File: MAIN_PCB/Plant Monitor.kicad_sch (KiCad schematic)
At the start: 59 parts, among them J1 TYPE-C-31-M-12, J2 Motor 1, J3 Motor 2, J4 Grove Connector for Soil Mois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, J5 Grove Connector for OLED Disp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, J6 Conn_01x14, J7 Conn_01x14, J8 JST PH-2Pin, J9 BME280 Terminals, Q1 AO3401A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

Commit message: Revision D of PCB design
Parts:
- U4: footprint Package_SON:Winbond_USON-8-1EP_3x2mm_P0.5mm_EP0.2x1.6mm -> Package_SO:SOIC-8_5.3x5.3mm_P1.27mm
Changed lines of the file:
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@@
 			)
 		)
-		(property "Footprint" "Package_SON:Winbond_USON-8-1EP_3x2mm_P0.5mm_EP0.2x1.6mm"
+		(property "Footprint" "Package_SO:SOIC-8_5.3x5.3mm_P1.27mm"
 			(at 321.31 218.44 0)
 			(hide yes)

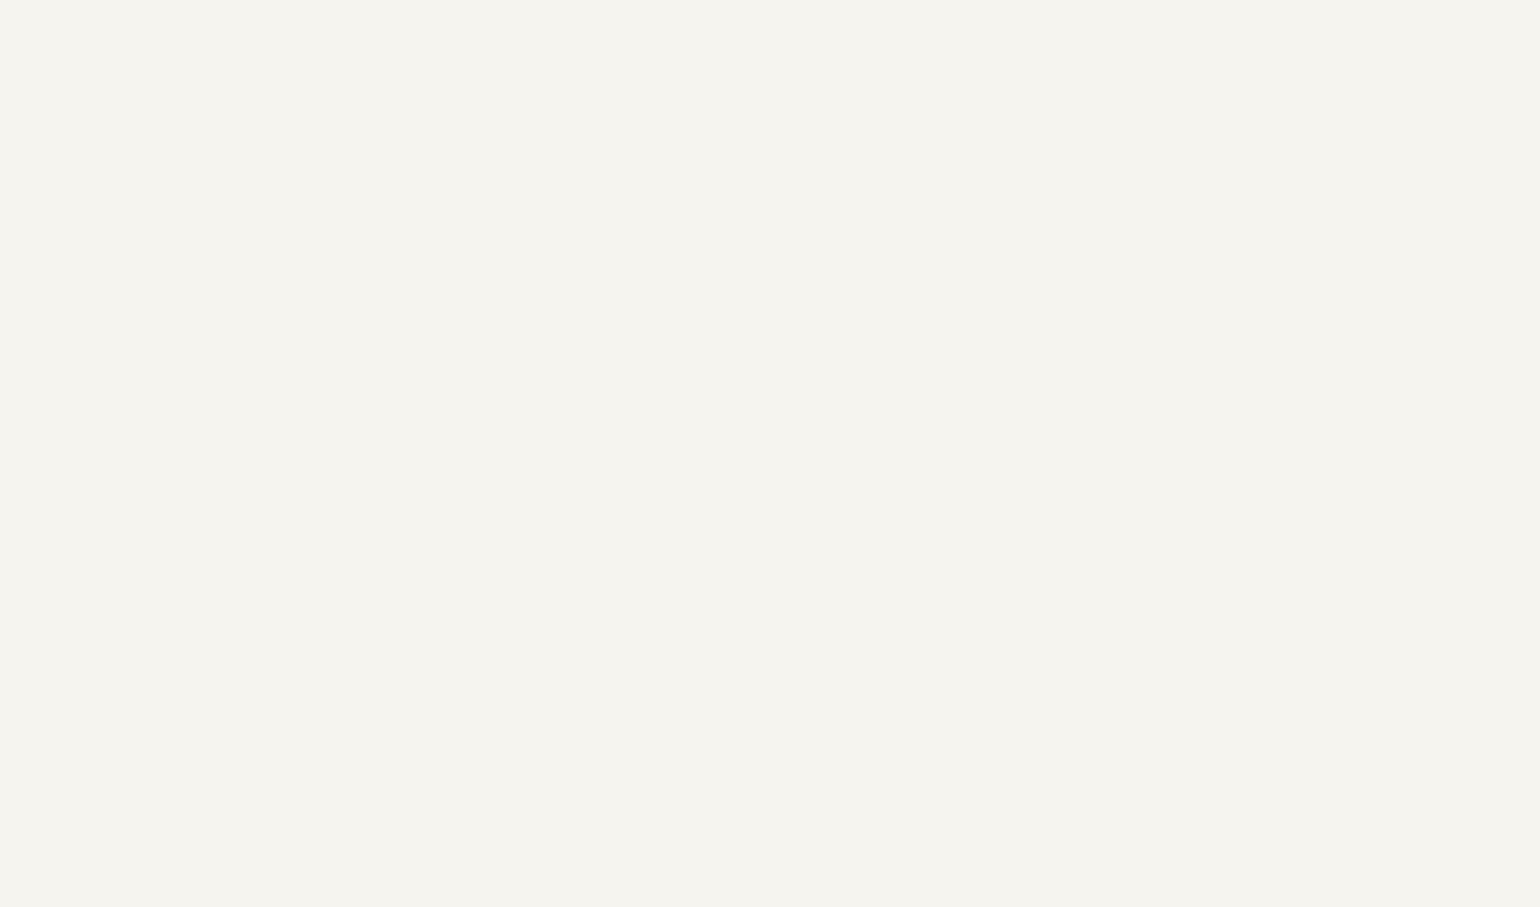
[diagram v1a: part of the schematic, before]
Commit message: Added wiring/schematic
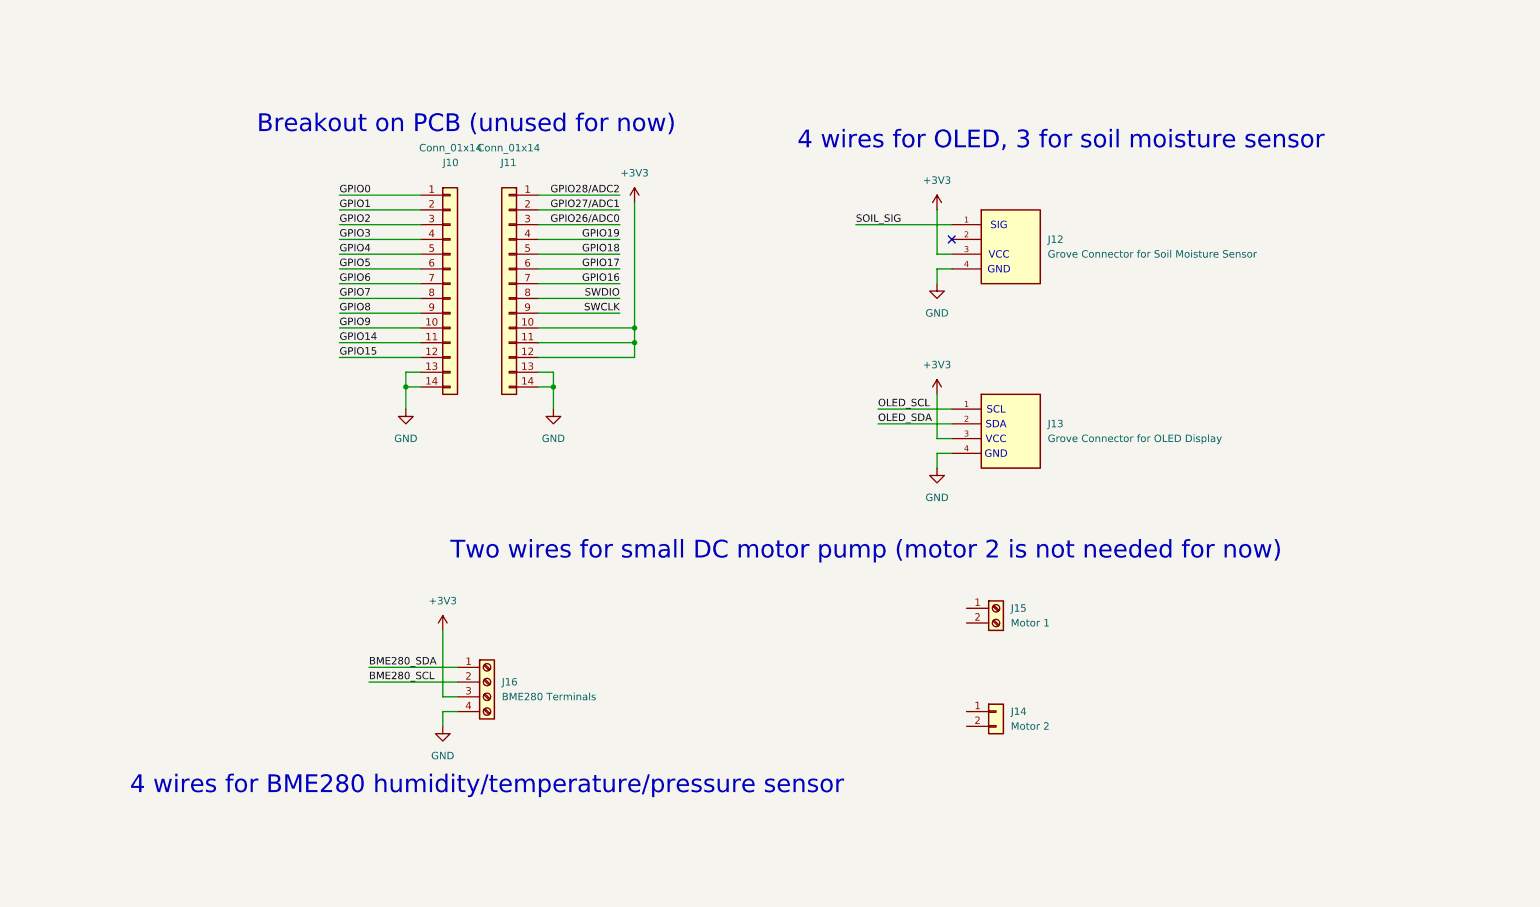
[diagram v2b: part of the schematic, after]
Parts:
- added J10, J11: Conn_01x14, Connector_PinHeader_2.54mm:PinHeader_1x14_P2.54mm_Vertical, symbol Connector_Generic:Conn_01x14
- added J12: Grove Connector for Soil Moisture Sensor, ExternalFootprints:SEEED_110990030, symbol Grove 4Pin Connector:110990030
- added J13: Grove Connector for OLED Display, ExternalFootprints:SEEED_110990030, symbol Grove 4Pin Connector:110990030
- added J14: Motor 2, Connector_PinHeader_2.54mm:PinHeader_1x02_P2.54mm_Vertical, symbol Connector_Generic:Conn_01x02
- added J15: Motor 1, TerminalBlock_Phoenix:TerminalBlock_Phoenix_MKDS-1,5-2-5.08_1x02_P5.08mm_Horizontal, symbol Connector:Screw_Terminal_01x02
- added J16: BME280 Terminals, TerminalBlock_Phoenix:TerminalBlock_Phoenix_MKDS-1,5-4_1x04_P5.00mm_Horizontal, symbol Connector:Screw_Terminal_01x04
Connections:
- net +3V3: now also J11.10 (Pin_10), J11.11 (Pin_11), J11.12 (Pin_12), J12.3, J13.3, J16.3 (Pin_3)
- net BME280_SCL: now also J16.2 (Pin_2)
- net BME280_SDA: now also J16.1 (Pin_1)
- net GND: now also J10.13 (Pin_13), J10.14 (Pin_14), J11.13 (Pin_13), J11.14 (Pin_14), J12.4, J13.4, J16.4 (Pin_4)
- net GPIO0: now also J10.1 (Pin_1)
- net GPIO1: now also J10.2 (Pin_2)
- net GPIO14: now also J10.11 (Pin_11)
- net GPIO15: now also J10.12 (Pin_12)
- net GPIO16: now also J11.7 (Pin_7)
- net GPIO17: now also J11.6 (Pin_6)
- net GPIO18: now also J11.5 (Pin_5)
- net GPIO19: now also J11.4 (Pin_4)
- net GPIO2: now also J10.3 (Pin_3)
- net GPIO26/ADC0: now also J11.3 (Pin_3)
- net GPIO27/ADC1: now also J11.2 (Pin_2)
- net GPIO28/ADC2: now also J11.1 (Pin_1)
- net GPIO3: now also J10.4 (Pin_4)
- net GPIO4: now also J10.5 (Pin_5)
- net GPIO5: now also J10.6 (Pin_6)
- net GPIO6: now also J10.7 (Pin_7)
- net GPIO7: now also J10.8 (Pin_8)
- net GPIO8: now also J10.9 (Pin_9)
- net GPIO9: now also J10.10 (Pin_10)
- net OLED_SCL: now also J13.1
- net OLED_SDA: now also J13.2
- net SOIL_SIG: now also J12.1
- net SWCLK: now also J11.9 (Pin_9)
- net SWDIO: now also J11.8 (Pin_8)
- no-connect marks 3 -> 4
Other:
- note added: "4 wires for BME280 humidity/temperature/pressure sensor"
- note added: "4 wires for OLED, 3 for soil moisture sensor"
- note added: "Breakout on PCB (unused for now)"
- note added: "Two wires for small DC motor pump (motor 2 is not needed for now)"
